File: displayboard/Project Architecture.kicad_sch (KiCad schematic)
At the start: 0 parts

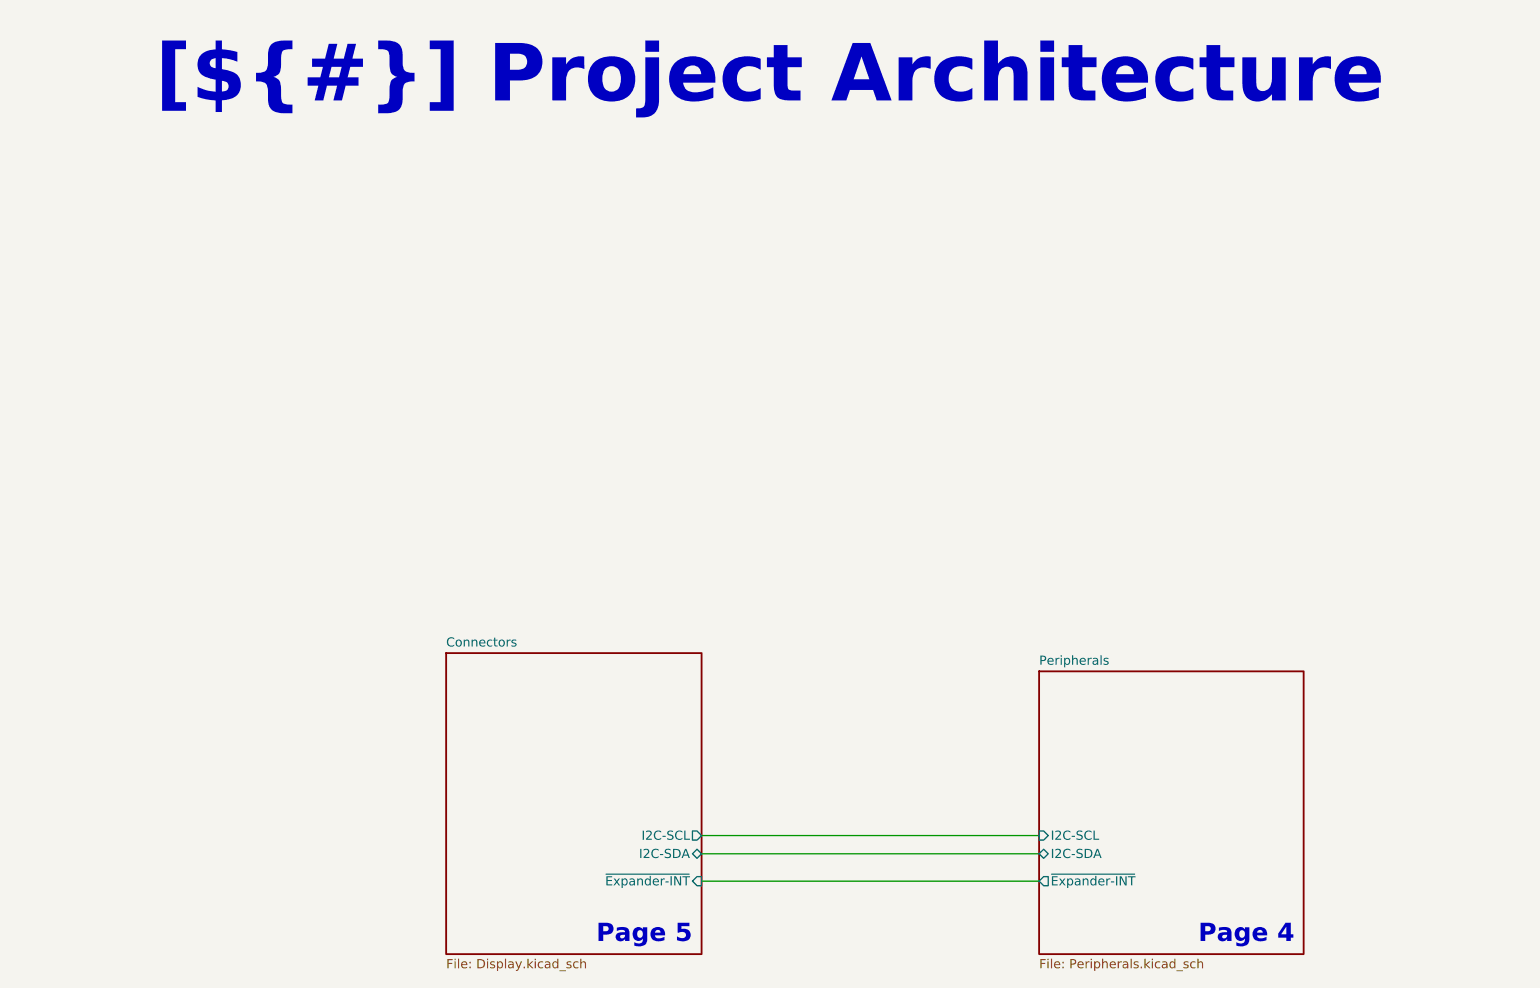
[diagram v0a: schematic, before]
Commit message: Remove old production files, add cutout for the programming cable, add connector for mainboard cable
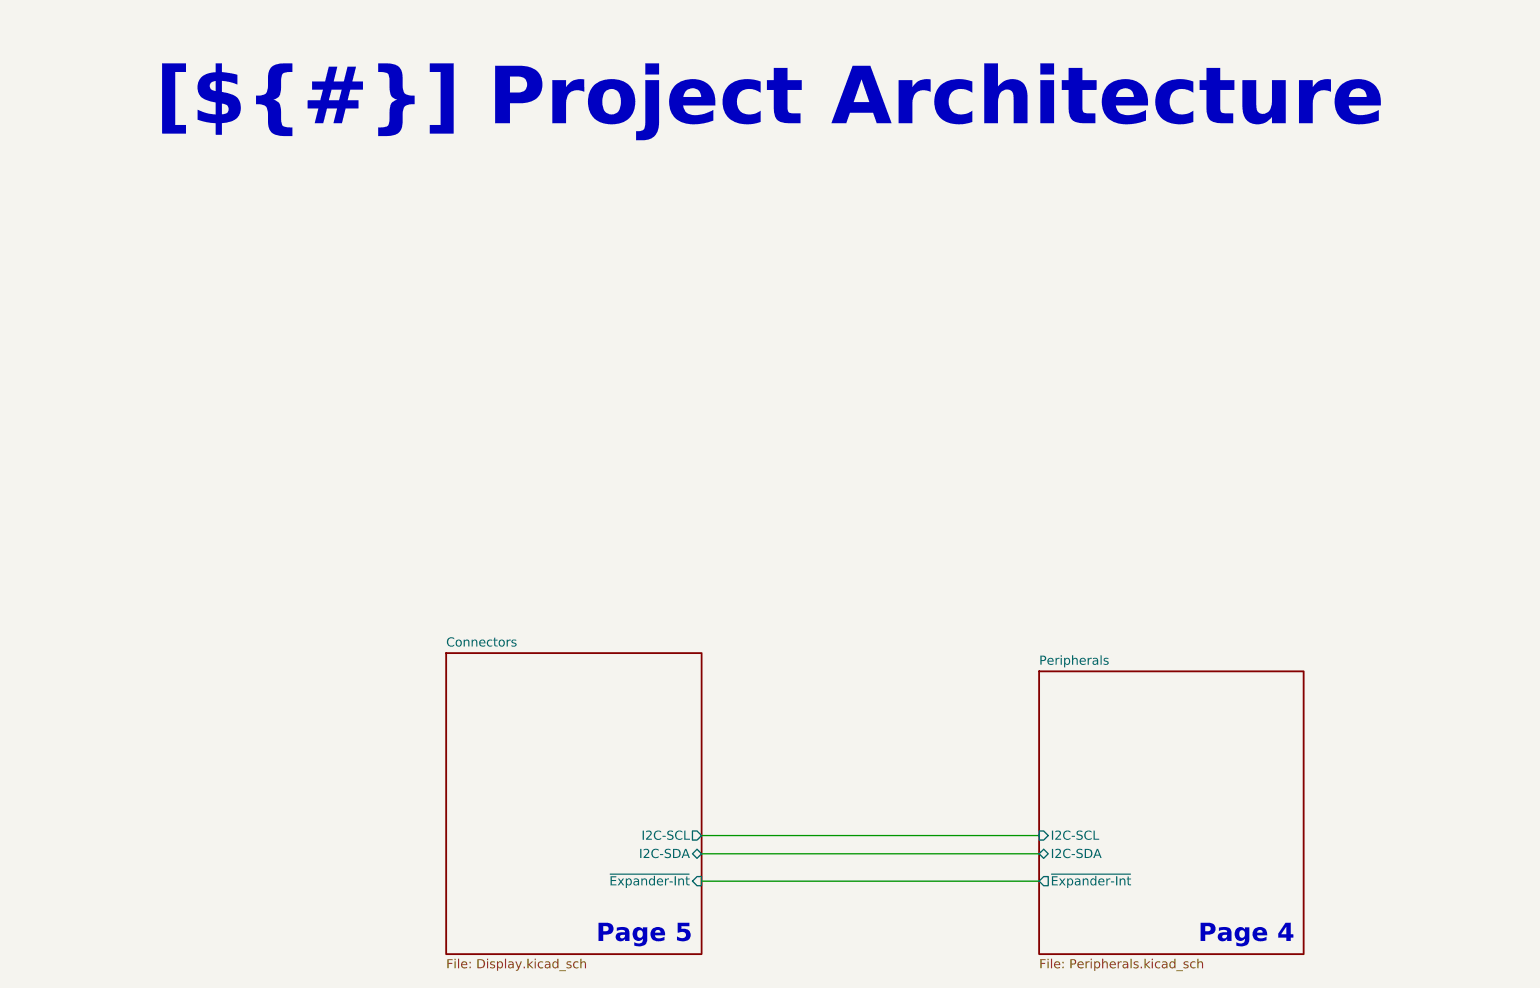
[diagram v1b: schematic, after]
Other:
- sheet Connectors ports: added ~{Expander-Int}; removed ~{Expander-INT}
- sheet Peripherals ports: added ~{Expander-Int}; removed ~{Expander-INT}
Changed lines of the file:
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@@
 		(exclude_from_sim no)
 		(at 12.7 12.7 0)
-		(size 394.97 13.97)
+		(size 394.97 20.32)
 		(margins 5.9999 5.9999 5.9999 5.9999)
 		(stroke
@@
 			)
 		)
-		(pin "~{Expander-INT}" input
+		(pin "~{Expander-Int}" input
 			(at 200.66 132.08 0)
 			(effects
@@
 			)
 		)
-		(pin "~{Expander-INT}" output
+		(pin "~{Expander-Int}" output
 			(at 247.65 132.08 180)
 			(effects
